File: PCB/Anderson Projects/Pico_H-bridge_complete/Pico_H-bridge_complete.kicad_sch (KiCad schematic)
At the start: 47 parts, among them J1 Screw_Terminal_01x10, J2 Motor Connector, J3 Screw_Terminal_01x02, SW1 SW_DIP_x01, U1 Pico, U5 OPA4197, U6 LM7810, U7 LM78L05

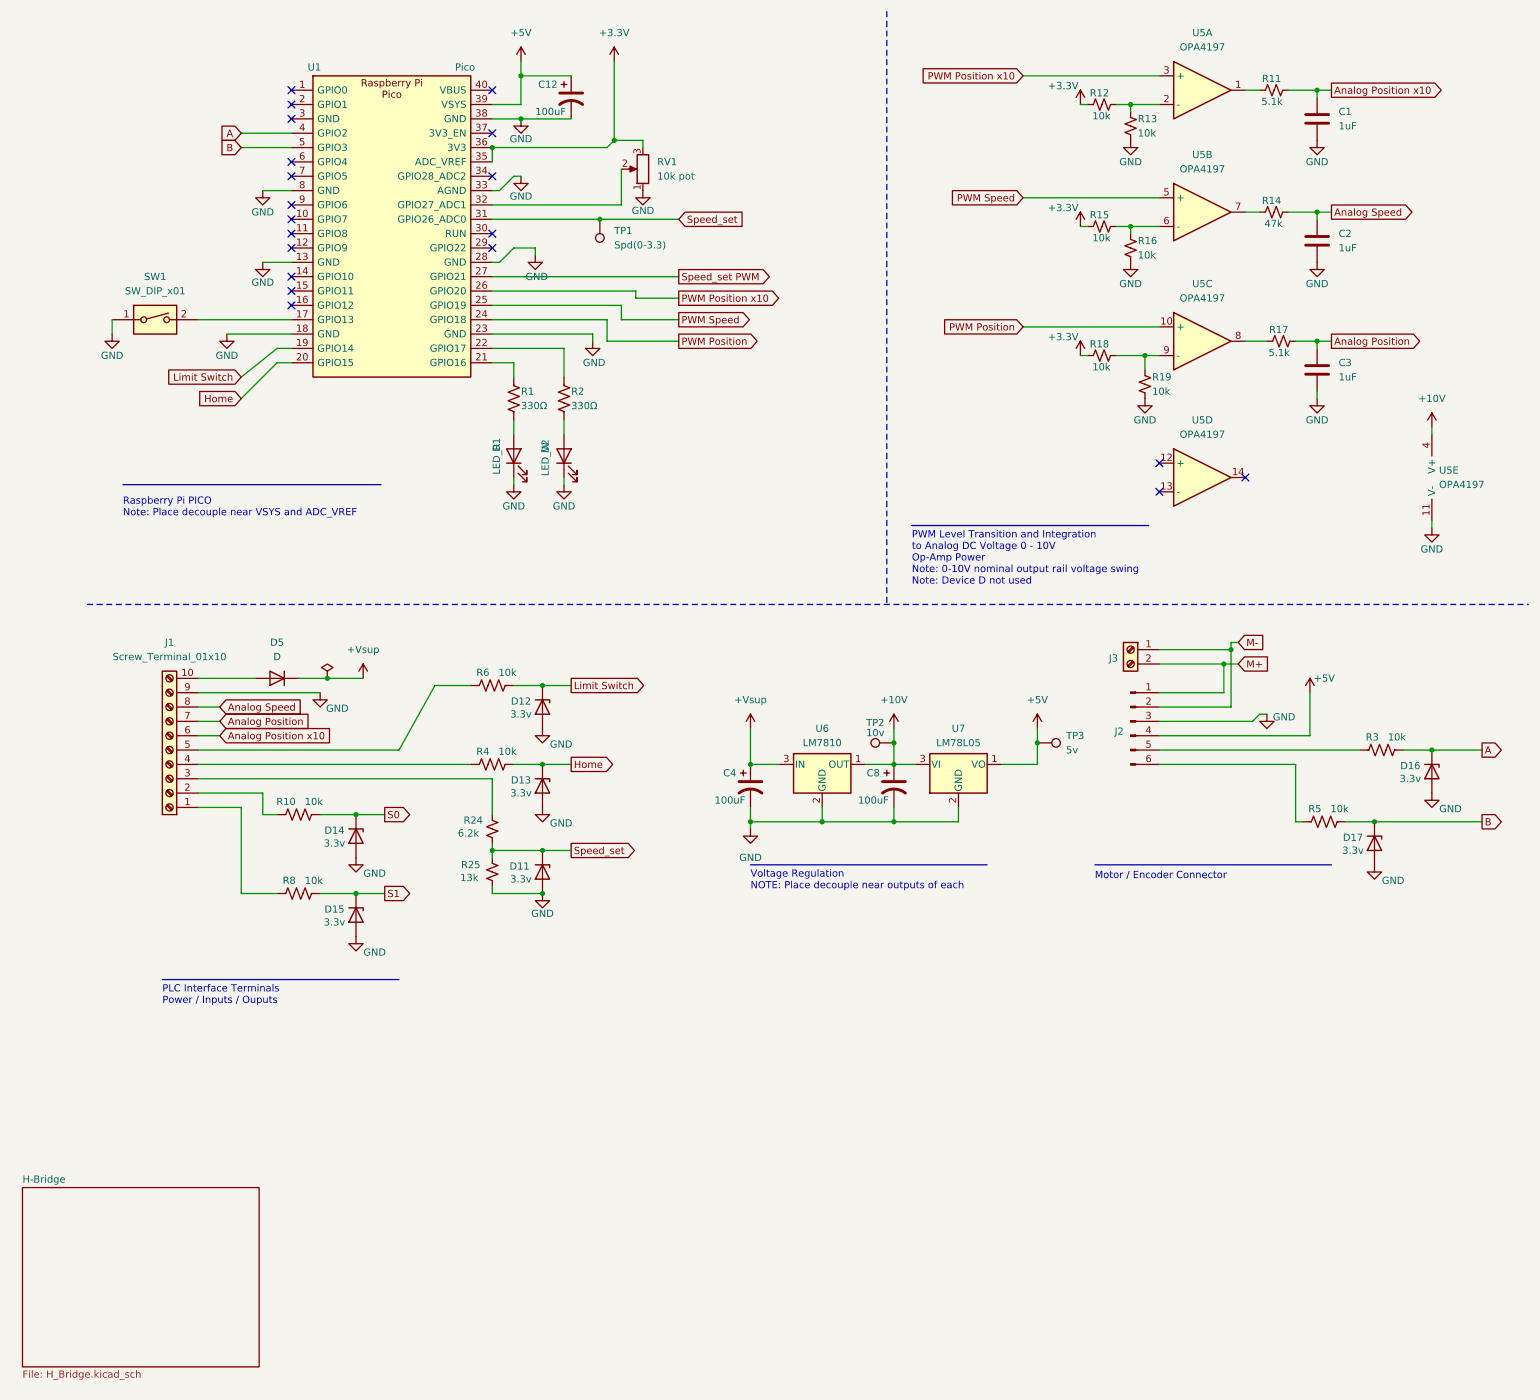
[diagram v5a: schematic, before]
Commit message: Updated Anderson Schematic to fix V0 issues
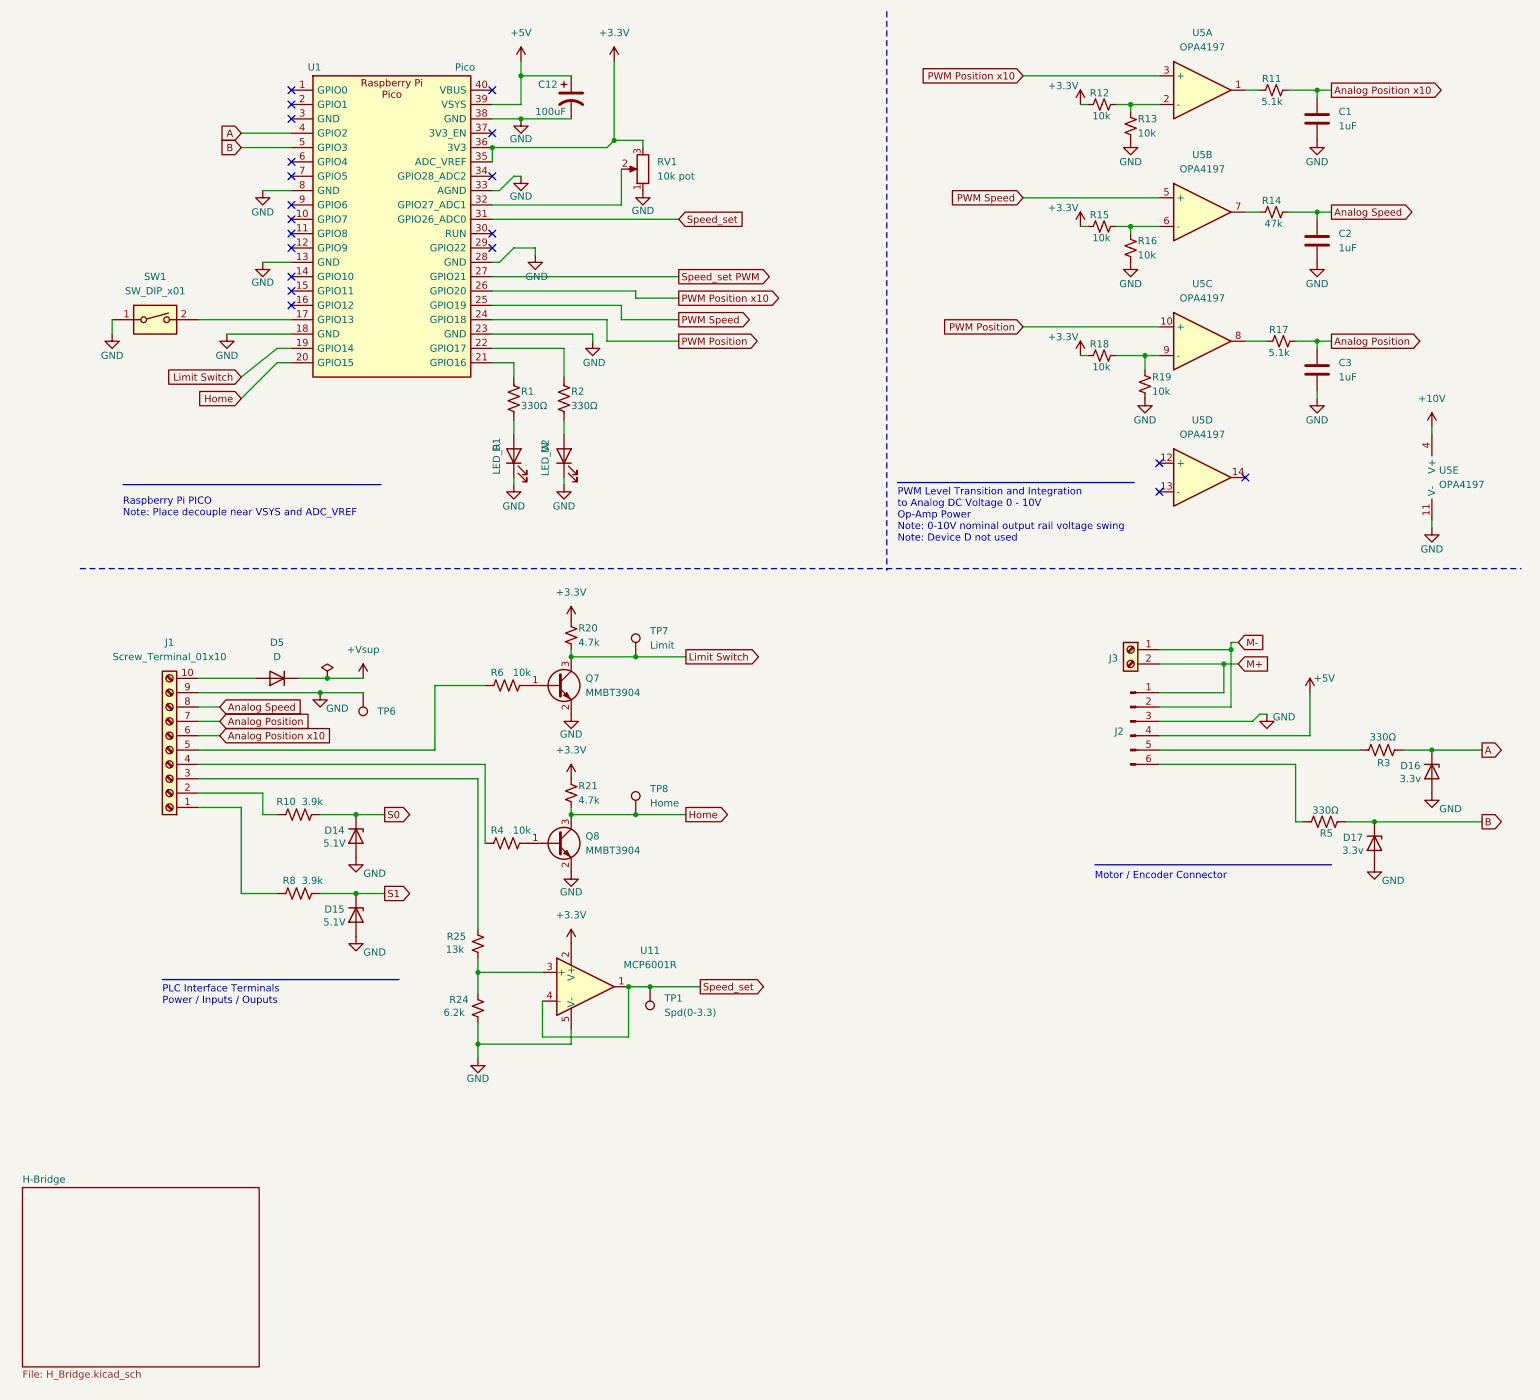
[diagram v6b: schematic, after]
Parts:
- removed C4, C8: 100uF, Capacitor_SMD:C_1210_3225Metric, symbol Device:C_Polarized_US
- removed D11, D12, D13: 3.3v, Diode_SMD:D_SOD-323, symbol Diode:Z1SMAxxx
- removed TP2: 10v, TestPoint:TestPoint_Plated_Hole_D2.0mm, symbol Connector:TestPoint
- removed TP3: 5v, TestPoint:TestPoint_Plated_Hole_D2.0mm, symbol Connector:TestPoint
- removed U6: LM7810, Package_TO_SOT_SMD:SOT-89-3, symbol Regulator_Linear:L78L10_SOT89
- removed U7: LM78L05, Package_TO_SOT_SMD:SOT-89-3, symbol Regulator_Linear:LM78L05_TO92
- added Q7, Q8: MMBT3904, Package_TO_SOT_SMD:SOT-23, symbol Transistor_BJT:MMBT3904
- added R20, R21: 4.7k, Resistor_SMD:R_0603_1608Metric, symbol Device:R_Small_US
- added TP6: GND, TestPoint:TestPoint_Loop_D2.60mm_Drill1.4mm_Beaded, symbol Connector:TestPoint
- added TP7: Limit, TestPoint:TestPoint_Plated_Hole_D2.0mm, symbol Connector:TestPoint
- added TP8: Home, TestPoint:TestPoint_Plated_Hole_D2.0mm, symbol Connector:TestPoint
- added U11: MCP6001R, Package_TO_SOT_SMD:SOT-23-5, symbol Amplifier_Operational:MCP6001R
- D14, D15: value 3.3v -> 5.1V; LCSC C19077437 -> C2118
- R10, R8: value 10k -> 3.9k; footprint Resistor_SMD:R_0603_1608Metric -> Resistor_SMD:R_0805_2012Metric; LCSC C25804 -> C17614; digikey https://www.digikey.com/en/products/detail/stackpole-electr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 -> https://jlcpcb.com/partdetail/18302-0805W8F3901T5E/C17614
- R3, R5: value 10k -> 330Ω; LCSC C25804 -> C23138; digikey https://www.digikey.com/en/products/detail/stackpole-electr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 -> (none)
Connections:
- net +3.3V: now also R20.1, R21.1, U11.2 (V+)
- net GND: now also R24.2, Q7.2 (E), Q8.2 (E), TP6.1, U11.5 (V-); no longer R25.2
- net Home: now also Q8.3 (C), R21.2, TP8.1; no longer R4.2
- net Limit Switch: now also Q7.3 (C), R20.2, TP7.1; no longer R6.2
- net Speed_set: now also U11.1, U11.4 (-); no longer R24.2, R25.1
- net at J1.3 (Pin_3): now also R25.1; no longer R24.1
- new net: R24.1, R25.2, U11.3 (+)
- new net: Q7.1 (B), R6.2
- new net: Q8.1 (B), R4.2
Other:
- note removed: "Voltage Regulation NOTE: Place decouple near outputs of each"
- moved on the sheet: R24, R25, R4, R6, TP1

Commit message: Final Board version prior to testing motor with pulleys. This version would not turn the motor when connected to a generator. The Vgs values for Mosfets needed increased to 10v. Other improvements to make include removing braking functionality to simplify control to Fwd/Rev vice S0/S1.
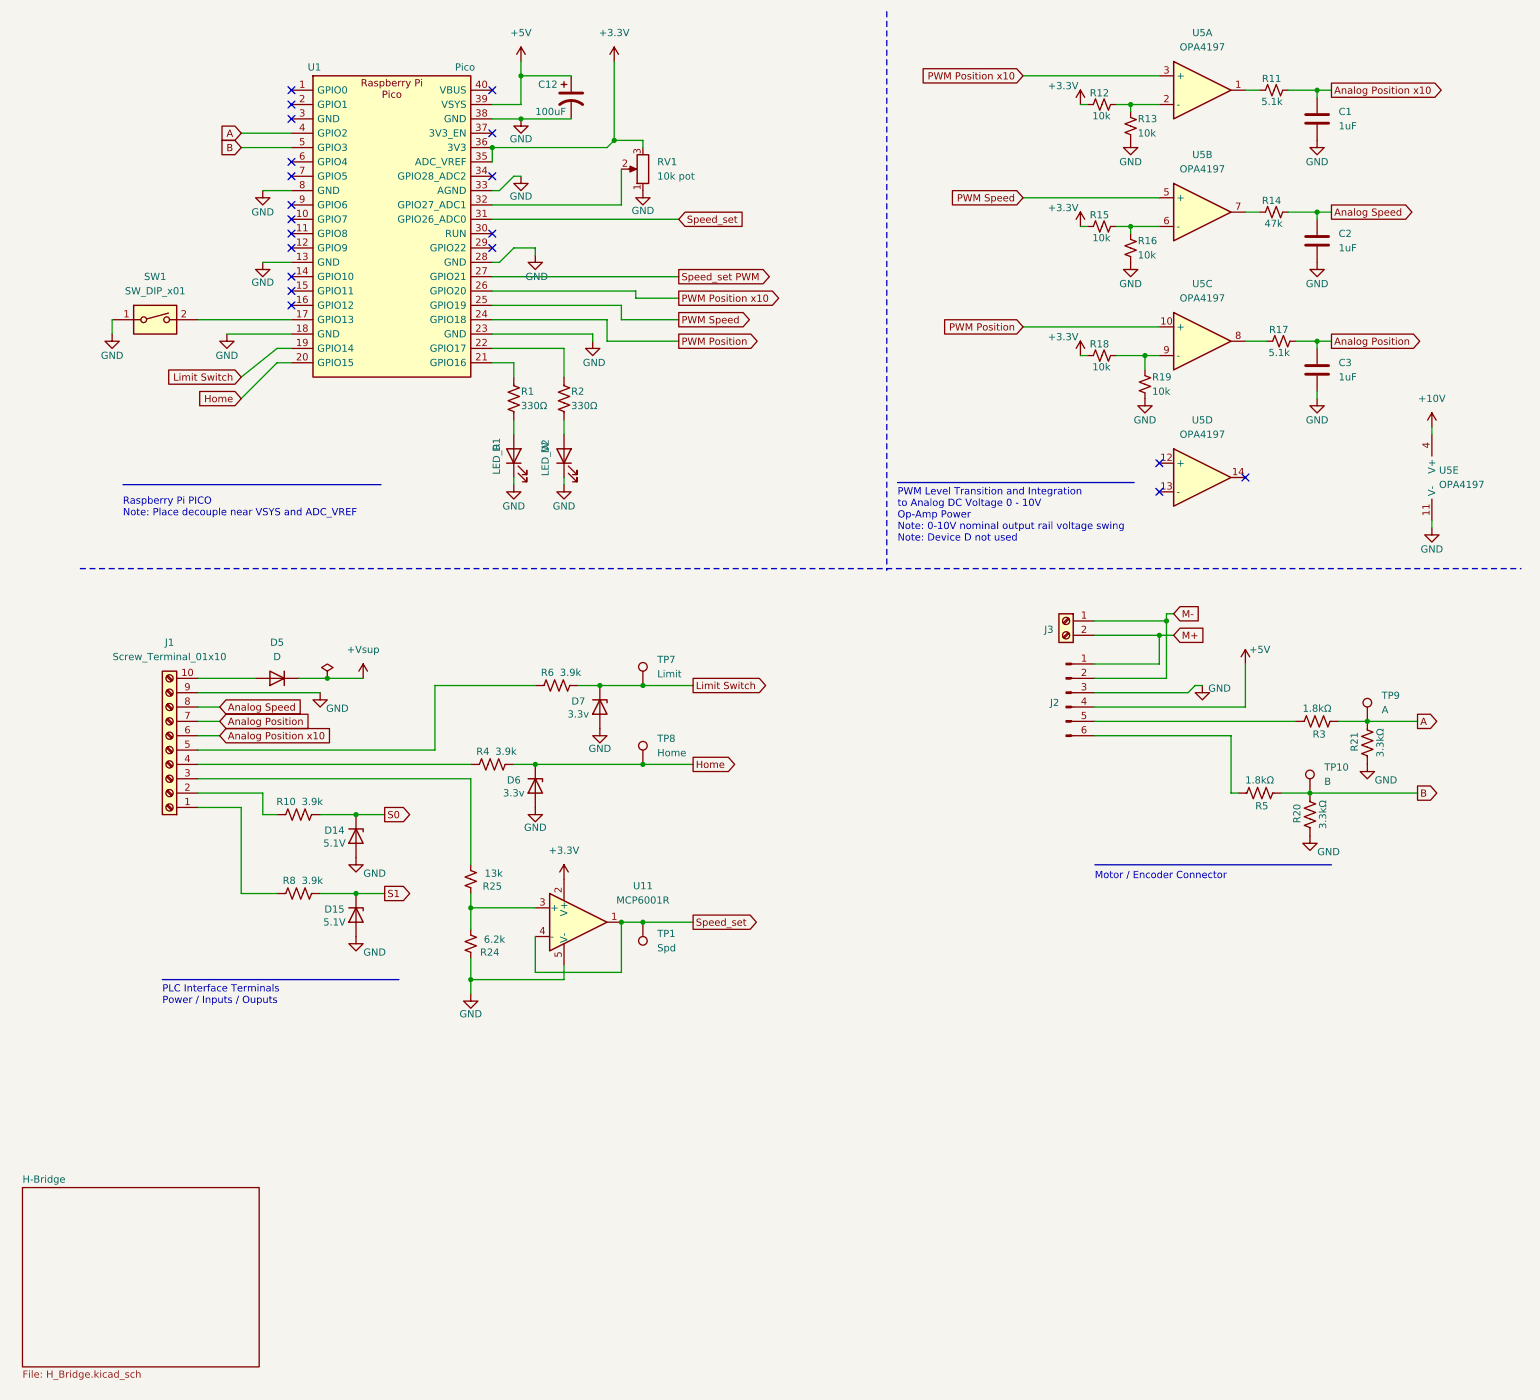
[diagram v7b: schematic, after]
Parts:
- removed D16, D17: 3.3v, Diode_SMD:D_SOD-323, symbol Diode:Z1SMAxxx
- removed Q7, Q8: MMBT3904, Package_TO_SOT_SMD:SOT-23, symbol Transistor_BJT:MMBT3904
- removed R20, R21: 4.7k, Resistor_SMD:R_0603_1608Metric, symbol Device:R_Small_US
- removed TP6: GND, TestPoint:TestPoint_Loop_D2.60mm_Drill1.4mm_Beaded, symbol Connector:TestPoint
- added D6, D7: 3.3v, Diode_SMD:D_SOD-323, symbol Diode:Z1SMAxxx
- added R20, R21: 3.3kΩ, Resistor_SMD:R_0603_1608Metric, symbol Device:R_US
- added TP10: B, TestPoint:TestPoint_Plated_Hole_D2.0mm, symbol Connector:TestPoint
- added TP9: A, TestPoint:TestPoint_Plated_Hole_D2.0mm, symbol Connector:TestPoint
- R10, R8: footprint Resistor_SMD:R_0805_2012Metric -> Resistor_SMD:R_0603_1608Metric; LCSC C17614 -> C23018; digikey https://jlcpcb.com/partdetail/18302-0805W8F3901T5E/C17614 -> (none)
- R3, R5: value 330Ω -> 1.8kΩ; LCSC C23138 -> C4177
- R4, R6: value 10k -> 3.9k; LCSC C25804 -> C23018; digikey https://www.digikey.com/en/products/detail/stackpole-electr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 -> (none)
- TP1: value Spd(0-3.3) -> Spd
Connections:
- net A: now also R21.1, TP9.1
- net B: now also R20.1, TP10.1
- net GND: now also R24.1, D6.2 (A), D7.2 (A), R20.2, R21.2; no longer R24.2
- net Home: now also R4.2, D6.1 (K)
- net Limit Switch: now also R6.2, D7.1 (K)
- net at J1.3 (Pin_3): now also R25.2; no longer R25.1
- new net: R24.2, R25.1, U11.3 (+)
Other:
- moved on the sheet: J2, J3, R24, R25, TP1, TP7, TP8, U11

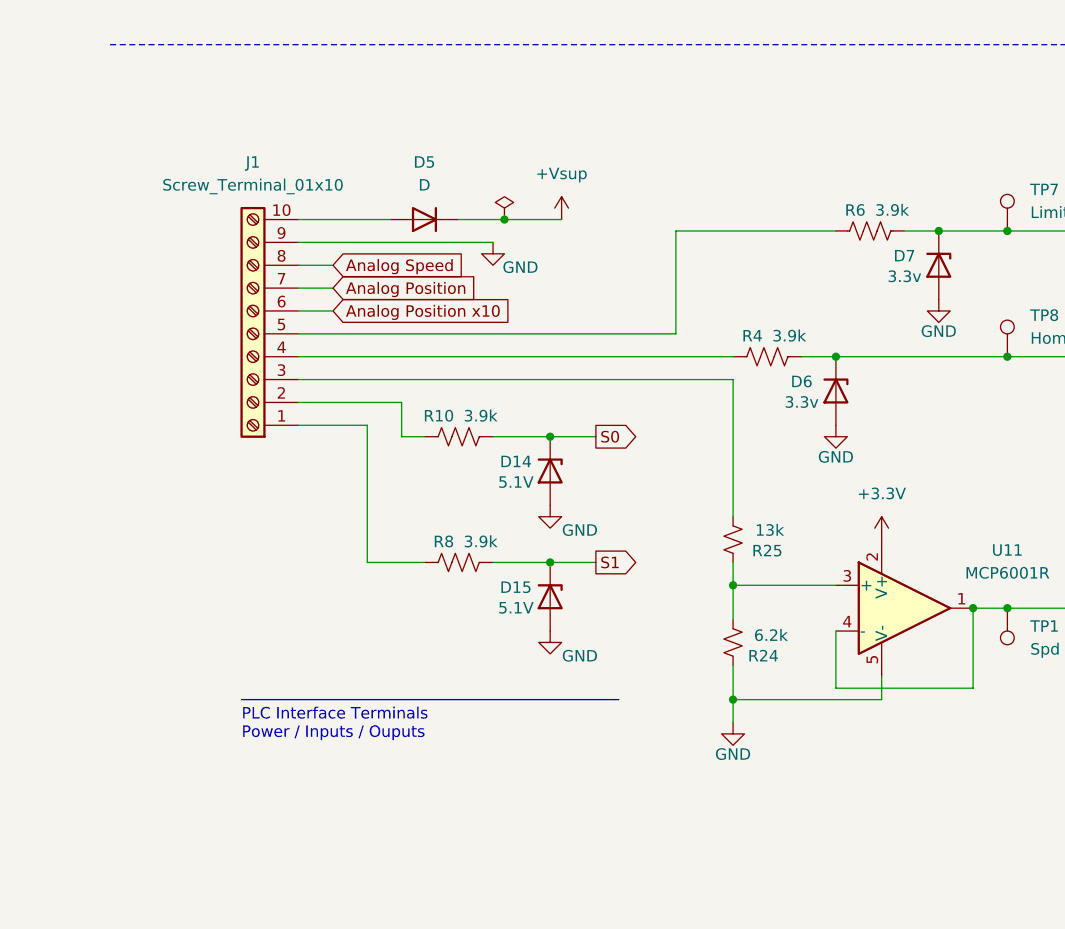
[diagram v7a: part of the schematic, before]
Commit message: (R's still mostly 0603)H-bridge circuit updated to achieve 10v Vgs. Replaced S0/S1 logic with Fwd/Rev simplified logic. Added header footprint for testing alternative capacitors. Minimized test points.
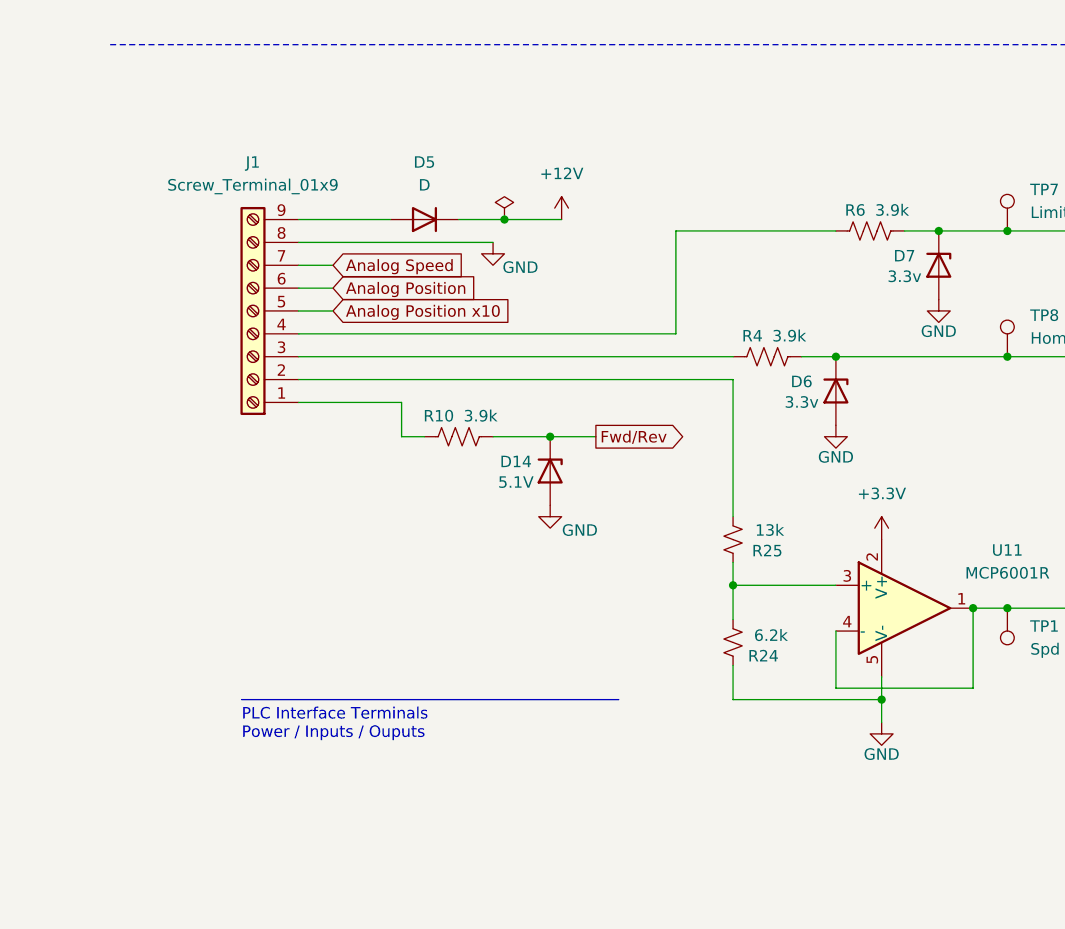
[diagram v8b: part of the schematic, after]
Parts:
- removed D15: 5.1V, Diode_SMD:D_SOD-323, symbol Diode:Z1SMAxxx
- removed R8: 3.9k, Resistor_SMD:R_0603_1608Metric, symbol Device:R_US
- J1: value Screw_Terminal_01x10 -> Screw_Terminal_01x9; symbol Connector:Screw_Terminal_01x10 -> Connector:Screw_Terminal_01x09
- R1, R2: LCSC C23138 -> C17630
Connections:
- net Analog Position: now also J1.6 (Pin_6); no longer J1.7 (Pin_7)
- net Analog Position x10: now also J1.5 (Pin_5); no longer J1.6 (Pin_6)
- net Analog Speed: now also J1.7 (Pin_7); no longer J1.8 (Pin_8)
- net GND: now also J1.8 (Pin_8); no longer J1.9 (Pin_9)
- net at J1.1 (Pin_1): now also R10.1
- net at D5.2 (A): now also J1.9 (Pin_9); no longer J1.10 (Pin_10)
- net at J1.2 (Pin_2): now also R25.2; no longer R10.1
- net at J1.3 (Pin_3): now also R4.1; no longer R25.2
- net at J1.4 (Pin_4): now also R6.1; no longer R4.1
- net +Vsup renamed +12V
- net S0 renamed Fwd/Rev
